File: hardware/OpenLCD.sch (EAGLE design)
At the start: 41 parts, among them Q1 PNP-500mA, Q2 PNP-500mA, Q3 PNP-500mA, U1 ATMEGA328P_TQFP, U2 4BIT-RGB, U3 MIC5205-ADJ, Y2 8MHz

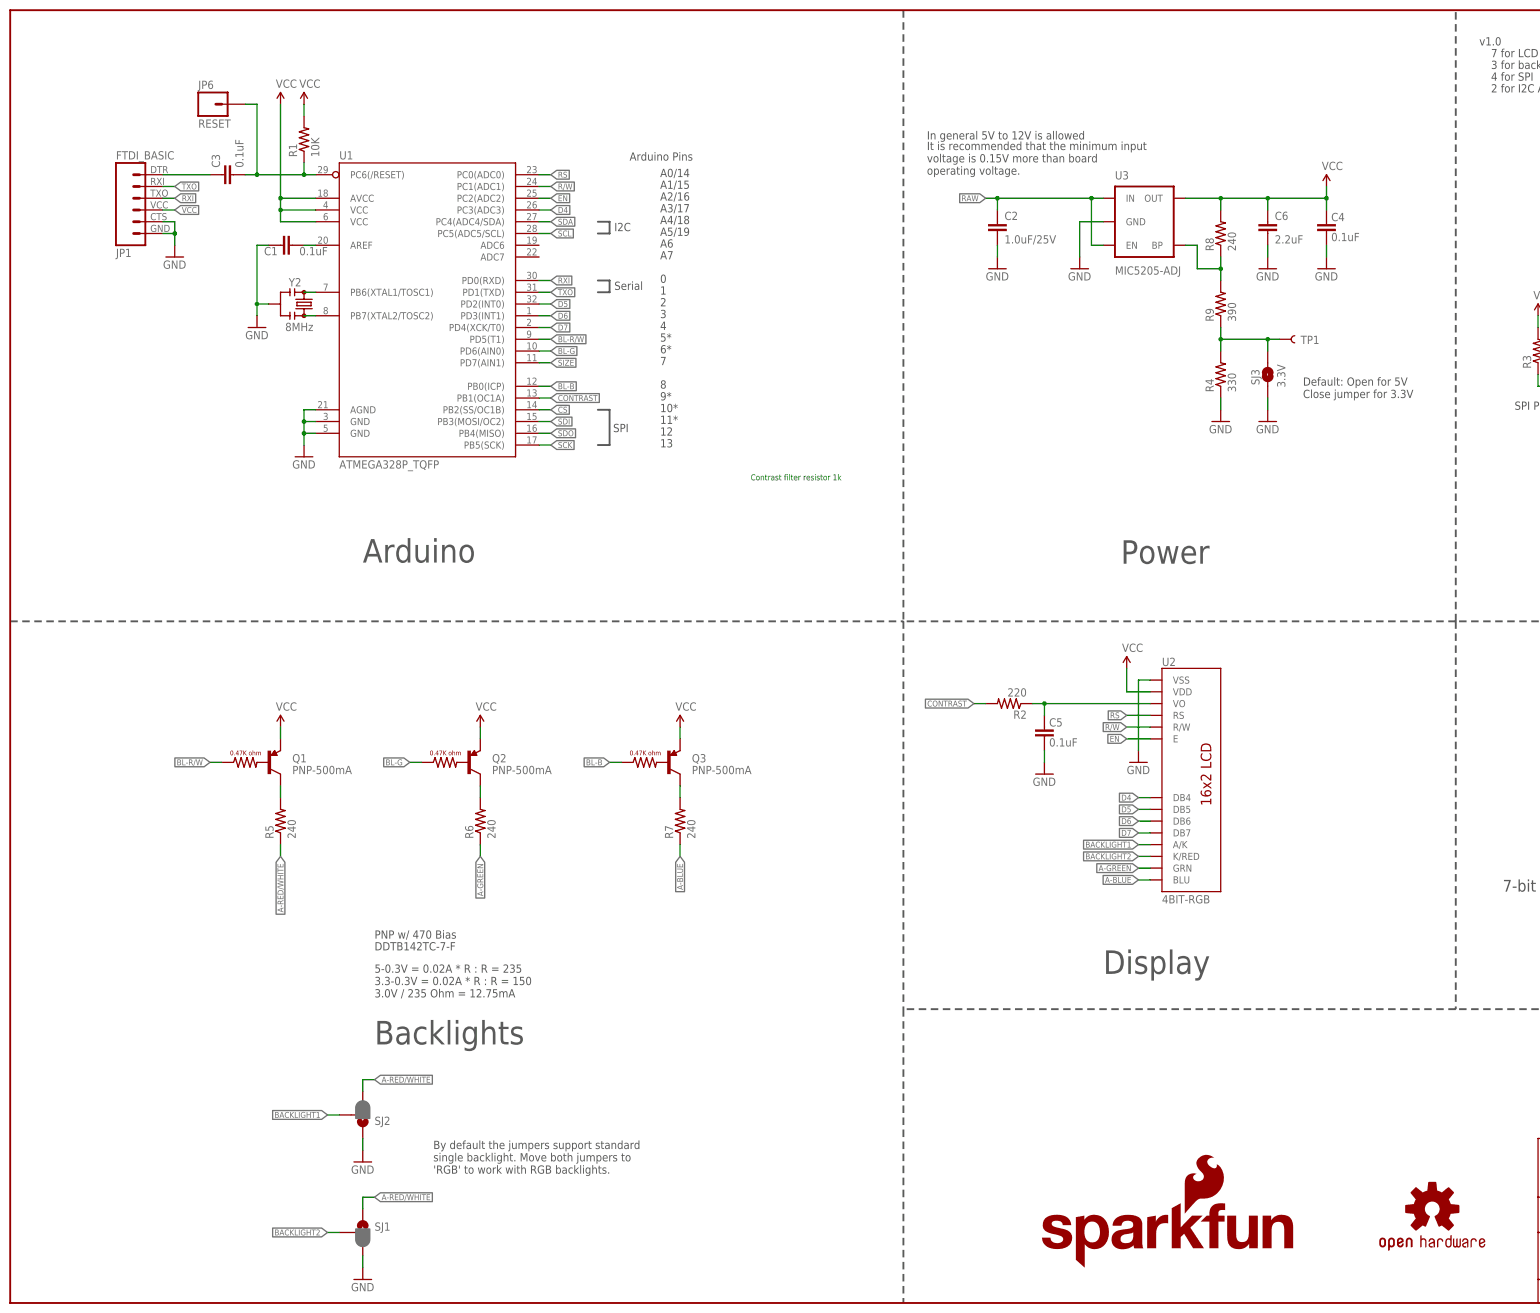
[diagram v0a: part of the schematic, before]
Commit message: Add back contrast trimpot. Add Bypass jumper.
Software contrast control is unreliable on too many types of LCDs.
Returned to a trimpot. Added a bypass jumper to allow for LCDs with
larger backlight requirements.
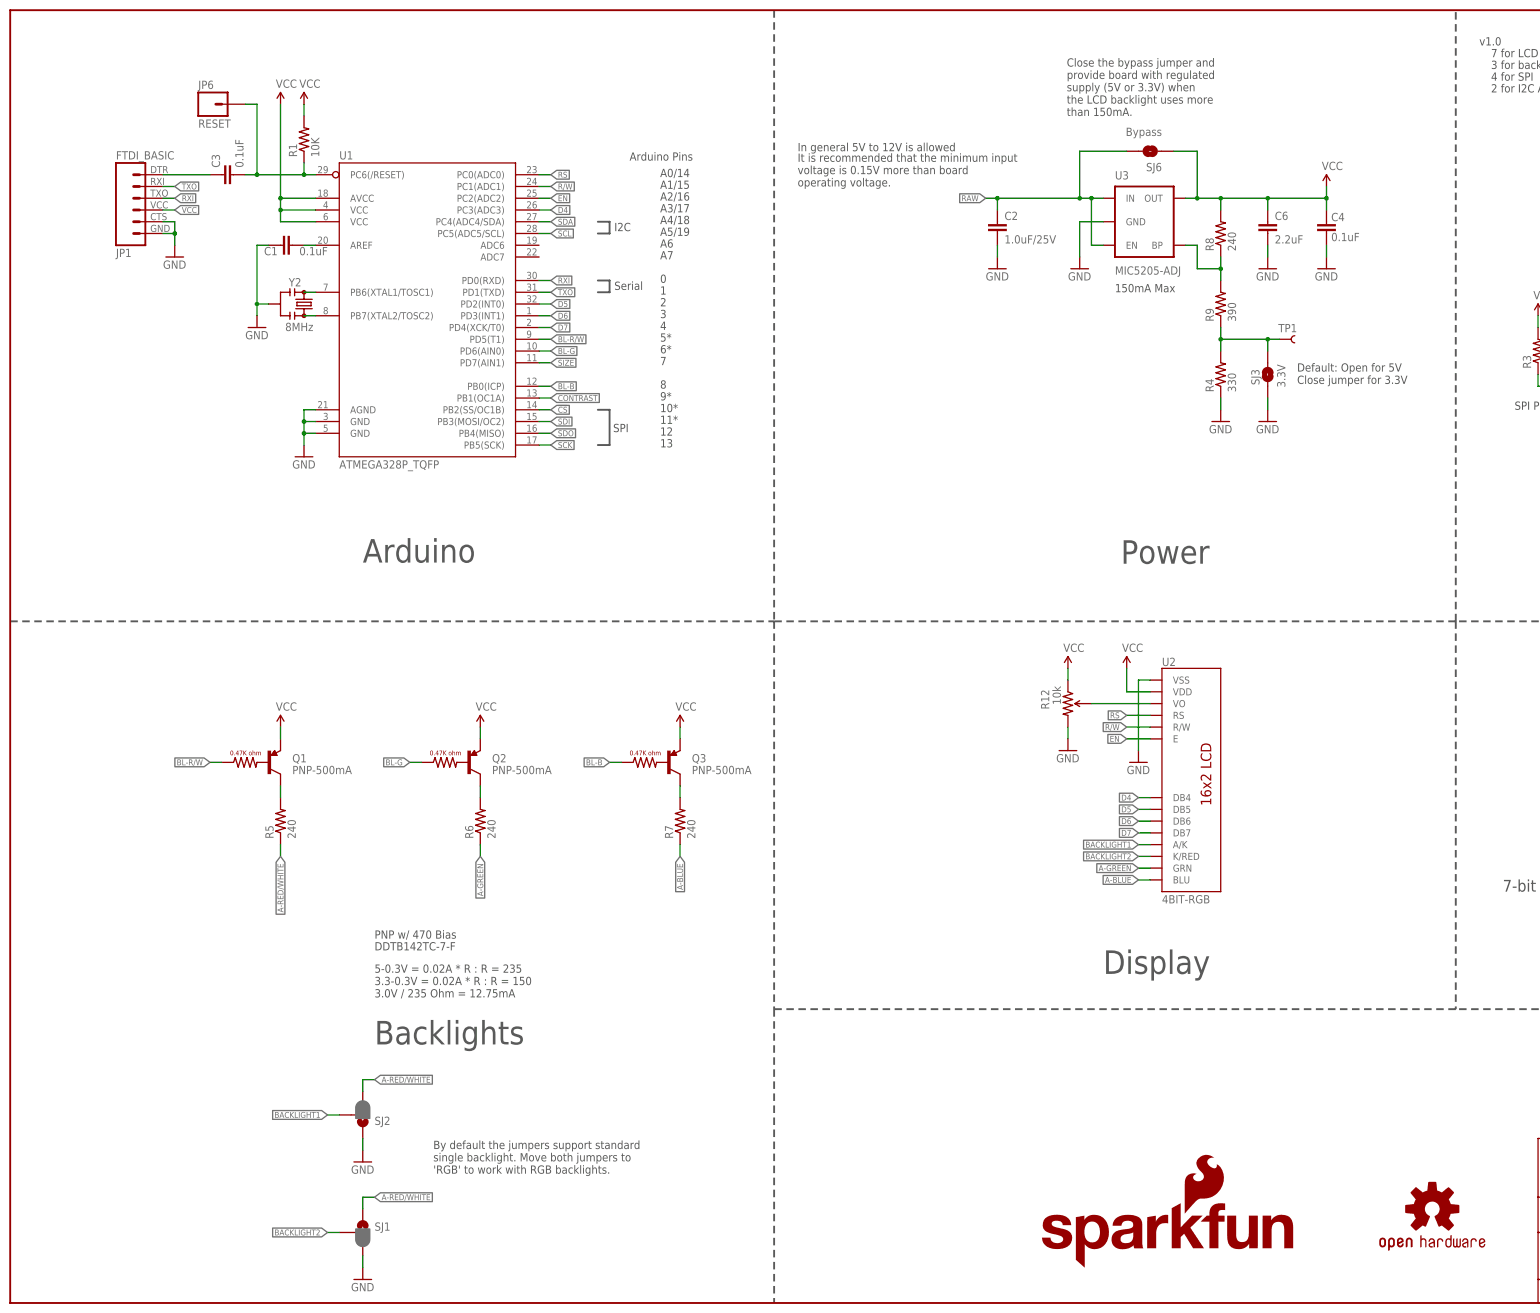
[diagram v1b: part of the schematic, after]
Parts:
- removed C5: 0.1uF, SparkFun-Capacitors:0.1UF-25V(+80/-20%)(0603)
- removed R2: 220, SparkFun-Resistors:10KOHM-1/10W-1%(0603)0603
- added R12: 10k, SparkFun-Electromechanical:TRIMPOTRES-09285
- added SJ6: Bypass, SparkFun-Passives:JUMPER-PAD-2-NOYES_SILK
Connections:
- net N$7 renamed 3.3V_CTRL
- removed net FILTERED_CONTRAST: C5.2, R2.1, U2.VO
- new net N$8: R12.WIPER, U2.VO
- net CONTRAST: no longer R2.2
- net GND: now also R12.CW; no longer C5.1
- net RAW: now also SJ6.2
- net VCC: now also R12.CCW, SJ6.1
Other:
- note added: "150mA Max"
- note added: "Close the bypass jumper and provide board with regulated supply (5V or 3.3V) when the LCD backlight uses more than 150mA."
- note removed: "Contrast filter resistor 1k"
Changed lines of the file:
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@@
 <?xml version="1.0" encoding="utf-8"?>
 <!DOCTYPE eagle SYSTEM "eagle.dtd">
-<eagle version="7.1.0">
+<eagle version="7.3.0">
 <drawing>
 <settings>
@@
 <part name="TP1" library="SparkFun-Passives" deviceset="TEST-POINT" device="3X4" value=""/>
 <part name="TP2" library="SparkFun-Passives" deviceset="TEST-POINT" device="3X4" value=""/>
-<part name="R2" library="SparkFun-Resistors" deviceset="10KOHM-1/10W-1%(0603)" device="0603" value="220"/>
-<part name="C5" library="SparkFun-Capacitors" deviceset="0.1UF-25V(+80/-20%)(0603)" device="" value="0.1uF"/>
+<part name="SJ6" library="SparkFun-Passives" deviceset="JUMPER-PAD-2-NO" device="YES_SILK" value="Bypass"/>
+<part name="R12" library="SparkFun-Electromechanical" deviceset="TRIMPOT" device="RES-09285" value="10k"/>
+<part name="P+8" library="SparkFun" deviceset="VCC" device=""/>
 <part name="GND12" library="SparkFun" deviceset="GND" device=""/>
 </parts>
@@
 <text x="140.462" y="228.092" size="1.778" layer="97">A6</text>
 <text x="140.462" y="225.552" size="1.778" layer="97">A7</text>
-<wire x1="0" y1="147.32" x2="193.04" y2="147.32" width="0.4064" layer="97" style="shortdash"/>
-<wire x1="193.04" y1="147.32" x2="193.04" y2="63.5" width="0.4064" layer="97" style="shortdash"/>
-<wire x1="193.04" y1="63.5" x2="193.04" y2="0" width="0.4064" layer="97" style="shortdash"/>
-<wire x1="193.04" y1="279.4" x2="193.04" y2="147.32" width="0.4064" layer="97" style="shortdash"/>
+<wire x1="0" y1="147.32" x2="165.1" y2="147.32" width="0.4064" layer="97" style="shortdash"/>
+<wire x1="165.1" y1="147.32" x2="165.1" y2="63.5" width="0.4064" layer="97" style="shortdash"/>
+<wire x1="165.1" y1="63.5" x2="165.1" y2="0" width="0.4064" layer="97" style="shortdash"/>
+<wire x1="165.1" y1="279.4" x2="165.1" y2="147.32" width="0.4064" layer="97" style="shortdash"/>
 <text x="76.2" y="160.02" size="5.08" layer="97" ratio="15">Arduino</text>
 <text x="236.22" y="71.12" size="5.08" layer="97" ratio="15">Display</text>
@@
 <text x="391.16" y="127" size="1.778" layer="97">5 to 12V Input</text>
 <wire x1="431.8" y1="147.32" x2="312.42" y2="147.32" width="0.4064" layer="97" style="shortdash"/>
-<wire x1="312.42" y1="147.32" x2="193.04" y2="147.32" width="0.4064" layer="97" style="shortdash"/>
+<wire x1="312.42" y1="147.32" x2="165.1" y2="147.32" width="0.4064" layer="97" style="shortdash"/>
 <wire x1="431.8" y1="63.5" x2="312.42" y2="63.5" width="0.4064" layer="97" style="shortdash"/>
 <text x="78.74" y="78.74" size="1.778" layer="97">PNP w/ 470 Bias</text>
@@
 3.3-0.3V = 0.02A * R : R = 150
 3.0V / 235 Ohm = 12.75mA</text>
-<text x="279.4" y="195.58" size="1.778" layer="97">Default: Open for 5V
+<text x="278.13" y="198.628" size="1.778" layer="97">Default: Open for 5V
 Close jumper for 3.3V</text>
 <text x="91.44" y="27.94" size="1.778" layer="97">By default the jumpers support standard
 single backlight. Move both jumpers to
 'RGB' to work with RGB backlights.</text>
-<wire x1="312.42" y1="63.5" x2="193.04" y2="63.5" width="0.4064" layer="97" style="shortdash"/>
+<wire x1="312.42" y1="63.5" x2="165.1" y2="63.5" width="0.4064" layer="97" style="shortdash"/>
 <wire x1="312.42" y1="147.32" x2="312.42" y2="63.5" width="0.4064" layer="97" style="shortdash"/>
 <wire x1="312.42" y1="147.32" x2="312.42" y2="279.4" width="0.4064" layer="97" style="shortdash"/>
@@
 Open jumper to remove I2C
 pull up resistors from bus</text>
-<text x="198.12" y="243.84" size="1.778" layer="97">It is recommended that the minimum input
+<text x="170.18" y="241.3" size="1.778" layer="97">It is recommended that the minimum input
 voltage is 0.15V more than board
 operating voltage.</text>
-<text x="198.12" y="251.46" size="1.778" layer="97">In general 5V to 12V is allowed</text>
-<text x="160.02" y="177.8" size="1.27" layer="91">Contrast filter resistor 1k</text>
+<text x="170.18" y="248.92" size="1.778" layer="97">In general 5V to 12V is allowed</text>
+<text x="228.346" y="256.54" size="1.778" layer="97">Close the bypass jumper and
+provide board with regulated
+supply (5V or 3.3V) when
+the LCD backlight uses more
+than 150mA.</text>
+<text x="238.76" y="218.44" size="1.778" layer="97">150mA Max</text>
 </plain>
 <instances>
@@
 <instance part="GND10" gate="1" x="76.2" y="5.08"/>
 <instance part="TP1" gate="G$1" x="274.32" y="208.28" smashed="yes">
-<attribute name="NAME" x="282.956" y="209.042" size="1.778" layer="95" rot="R180"/>
+<attribute name="NAME" x="274.066" y="209.804" size="1.778" layer="95"/>
 <attribute name="VALUE" x="271.78" y="205.74" size="1.778" layer="96"/>
 </instance>
@@
 <attribute name="VALUE" x="398.78" y="210.82" size="1.778" layer="96" rot="R180"/>
 </instance>
-<instance part="R2" gate="G$1" x="215.9" y="129.54" rot="R180"/>
-<instance part="C5" gate="G$1" x="223.52" y="124.46" smashed="yes" rot="R180">
-<attribute name="NAME" x="224.536" y="124.587" size="1.778" layer="95"/>
-<attribute name="VALUE" x="224.536" y="120.269" size="1.778" layer="96"/>
+<instance part="SJ6" gate="G$1" x="246.38" y="248.92" rot="R180"/>
+<instance part="R12" gate="R?" x="228.6" y="129.54" smashed="yes" rot="R270">
+<attribute name="NAME" x="224.5614" y="128.27" size="1.778" layer="95" rot="R90"/>
+<attribute name="VALUE" x="225.298" y="133.35" size="1.778" layer="96" rot="R270"/>
 </instance>
-<instance part="GND12" gate="1" x="223.52" y="114.3"/>
+<instance part="P+8" gate="1" x="228.6" y="137.16"/>
+<instance part="GND12" gate="1" x="228.6" y="119.38"/>
 </instances>
 <busses>
@@
 </segment>
 <segment>
-<pinref part="C5" gate="G$1" pin="1"/>
+<pinref part="R12" gate="R?" pin="CW"/>
 <pinref part="GND12" gate="1" pin="GND"/>
-<wire x1="223.52" y1="116.84" x2="223.52" y2="119.38" width="0.1524" layer="91"/>
+<wire x1="228.6" y1="121.92" x2="228.6" y2="124.46" width="0.1524" layer="91"/>
 </segment>
 </net>
@@
 </segment>
 <segment>
-<wire x1="254" y1="238.76" x2="261.62" y2="238.76" width="0.1524" layer="91"/>
+<wire x1="254" y1="238.76" x2="256.54" y2="238.76" width="0.1524" layer="91"/>
+<wire x1="256.54" y1="238.76" x2="261.62" y2="238.76" width="0.1524" layer="91"/>
 <wire x1="261.62" y1="238.76" x2="271.78" y2="238.76" width="0.1524" layer="91"/>
 <wire x1="271.78" y1="238.76" x2="271.78" y2="236.22" width="0.1524" layer="91"/>
@@
 <wire x1="284.48" y1="241.3" x2="284.48" y2="238.76" width="0.1524" layer="91"/>
 <junction x="284.48" y="238.76"/>
+<pinref part="SJ6" gate="G$1" pin="1"/>
+<wire x1="251.46" y1="248.92" x2="256.54" y2="248.92" width="0.1524" layer="91"/>
+<wire x1="256.54" y1="248.92" x2="256.54" y2="238.76" width="0.1524" layer="91"/>
+<junction x="256.54" y="238.76"/>
 </segment>
 <segment>
@@
 <wire x1="360.68" y1="215.9" x2="360.68" y2="213.36" width="0.1524" layer="91"/>
 </segment>
+<segment>
+<pinref part="R12" gate="R?" pin="CCW"/>
+<pinref part="P+8" gate="1" pin="VCC"/>
+<wire x1="228.6" y1="137.16" x2="228.6" y2="134.62" width="0.1524" layer="91"/>
+</segment>
 </net>
 <net name="SDI" class="0">
@@
 <wire x1="236.22" y1="228.6" x2="233.68" y2="228.6" width="0.1524" layer="91"/>
 <wire x1="233.68" y1="228.6" x2="233.68" y2="238.76" width="0.1524" layer="91"/>
-<wire x1="213.36" y1="238.76" x2="233.68" y2="238.76" width="0.1524" layer="91"/>
+<wire x1="213.36" y1="238.76" x2="231.14" y2="238.76" width="0.1524" layer="91"/>
+<wire x1="231.14" y1="238.76" x2="233.68" y2="238.76" width="0.1524" layer="91"/>
 <wire x1="213.36" y1="236.22" x2="213.36" y2="238.76" width="0.1524" layer="91"/>
 <wire x1="213.36" y1="238.76" x2="210.82" y2="238.76" width="0.1524" layer="91"/>
@@
 <pinref part="U3" gate="U1" pin="EN"/>
 <pinref part="C2" gate="G$1" pin="1"/>
+<pinref part="SJ6" gate="G$1" pin="2"/>
+<wire x1="241.3" y1="248.92" x2="231.14" y2="248.92" width="0.1524" layer="91"/>
+<wire x1="231.14" y1="248.92" x2="231.14" y2="238.76" width="0.1524" layer="91"/>
+<junction x="231.14" y="238.76"/>
 </segment>
 <segment>
@@
 <label x="116.84" y="195.58" size="1.27" layer="95" xref="yes"/>
 <pinref part="U1" gate="U$1" pin="PB1(OC1A)"/>
-</segment>
-<segment>
-<pinref part="R2" gate="G$1" pin="2"/>
-<wire x1="210.82" y1="129.54" x2="208.28" y2="129.54" width="0.1524" layer="91"/>
-<label x="208.28" y="129.54" size="1.27" layer="95" rot="R180" xref="yes"/>
 </segment>
 </net>
@@
 </segment>
 </net>
-<net name="N$7" class="0">
+<net name="3.3V_CTRL" class="0">
 <segment>
 <pinref part="R4" gate="G$1" pin="2"/>
@@
 </segment>
 </net>
-<net name="FILTERED_CONTRAST" class="0">
+<net name="N$8" class="0">
 <segment>
 <pinref part="U2" gate="U1" pin="VO"/>
-<pinref part="R2" gate="G$1" pin="1"/>
-<wire x1="220.98" y1="129.54" x2="223.52" y2="129.54" width="0.1524" layer="91"/>
-<pinref part="C5" gate="G$1" pin="2"/>
-<wire x1="223.52" y1="129.54" x2="246.38" y2="129.54" width="0.1524" layer="91"/>
-<wire x1="223.52" y1="127" x2="223.52" y2="129.54" width="0.1524" layer="91"/>
-<junction x="223.52" y="129.54"/>
-</segment>
-</net>
+<pinref part="R12" gate="R?" pin="WIPER"/>
+<wire x1="246.38" y1="129.54" x2="233.68" y2="129.54" width="0.1524" layer="91"/>
+</segment>
+</net>
